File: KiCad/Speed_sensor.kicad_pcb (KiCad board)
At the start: 4 copper layers, 35 x 20 mm, 65 parts, among them J1 USB_B_Micro, J2 SWD, U1 BQ24040DSQR, U2 TP1941U, U3 ST1PS02, U4 nRF52832-QFxx, U5 LIS2DH12, Y1 32,768kHz, Y2 32MHz

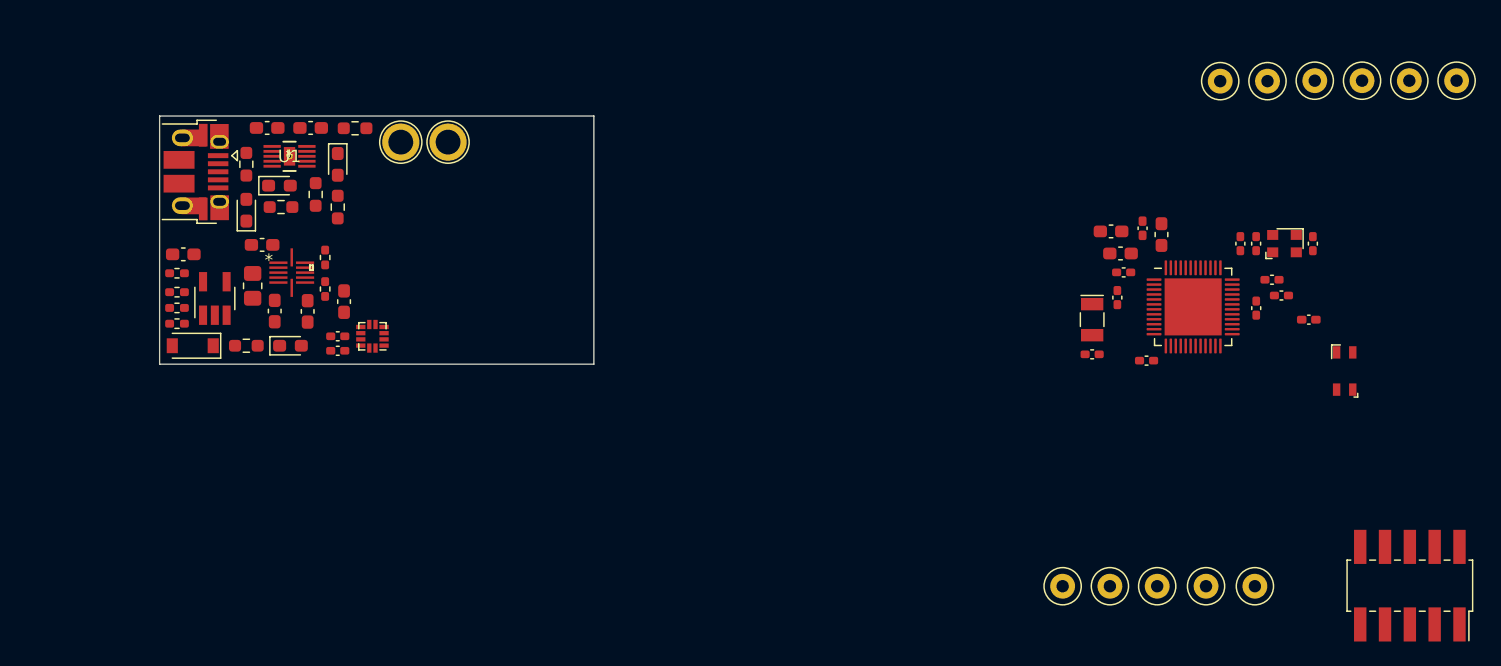
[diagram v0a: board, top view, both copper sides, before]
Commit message: kleine Änderungen an Bauteilplatzierungen um vias unterbringen zu können, 'keepout area' für Antenne eingefügt.
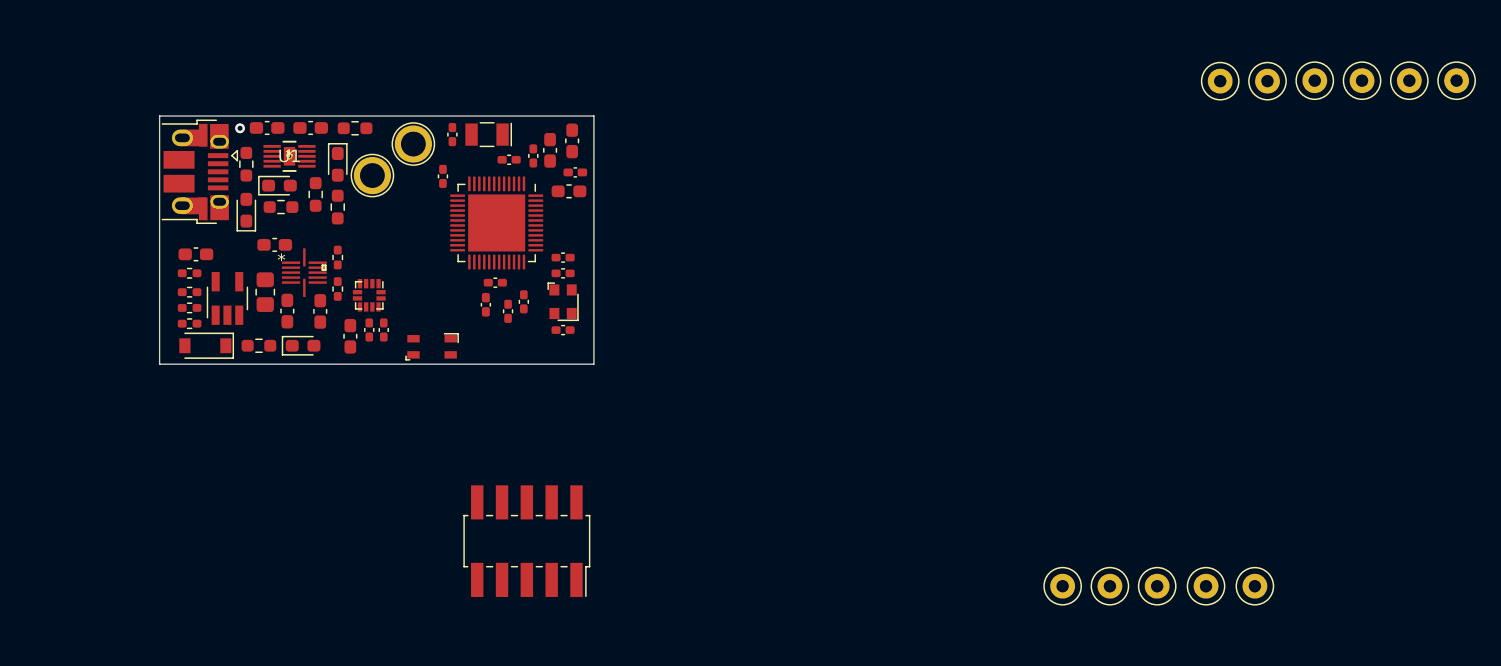
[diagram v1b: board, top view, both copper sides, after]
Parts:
- moved AE1 73.6 mm to (55.1, 55.0), turned to 180 degrees
- moved J2 71.3 mm to (62.7, 70.6)
- moved L4 66.3 mm to (59.4, 51.6), turned to 90 degrees
- moved C12 62.3 mm to (61.2, 52.1), turned to 270 degrees
- moved C17 61.4 mm to (60.2, 49.8), turned to 180 degrees
- moved C18 60.8 mm to (65.7, 53.6), turned to 180 degrees
- moved C11 60.3 mm to (62.5, 51.3), turned to 270 degrees
- moved C9 58.6 mm to (56.0, 41.2), turned to 90 degrees
- moved Y2 58.3 mm to (65.7, 51.3), turned to 90 degrees
- moved U4 56.5 mm to (60.3, 45.0), turned to 270 degrees
- moved C19 55.9 mm to (65.7, 49.0), turned to 0 degrees
- moved C10 54.6 mm to (65.7, 47.8), turned to 0 degrees
- moved C16 54.5 mm to (56.7, 37.8), turned to 90 degrees
- moved Y1 51.0 mm to (59.5, 37.8), turned to 180 degrees
- moved C15 50.3 mm to (61.3, 39.9), turned to 0 degrees
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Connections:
- U4 pad 15: Net-(U4-Pad15) -> SPI_MOSI
- U4 pad 16: SPI_MOSI -> SPI_MISO
- U4 pad 17: SPI_MISO -> SPI_01_CS
- U4 pad 18: SPI_01_CS -> SPI_SCK
- U4 pad 19: SPI_SCK -> ACCEL_INT1
- U4 pad 20: Net-(U4-Pad20) -> ACCEL_INT2
- U4 pad 8: ACCEL_INT1 -> Net-(U4-Pad8)
- U4 pad 9: ACCEL_INT2 -> Net-(U4-Pad9)
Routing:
- net +5V: vias 0 -> 1
- added copper zone on In2.Cu, net +3V0
- added copper zone on In1.Cu, net +5V
- added copper zone on In2.Cu, net +5V
- added copper zone on In2.Cu, net +BATT
- added copper zone on In1.Cu, net GND

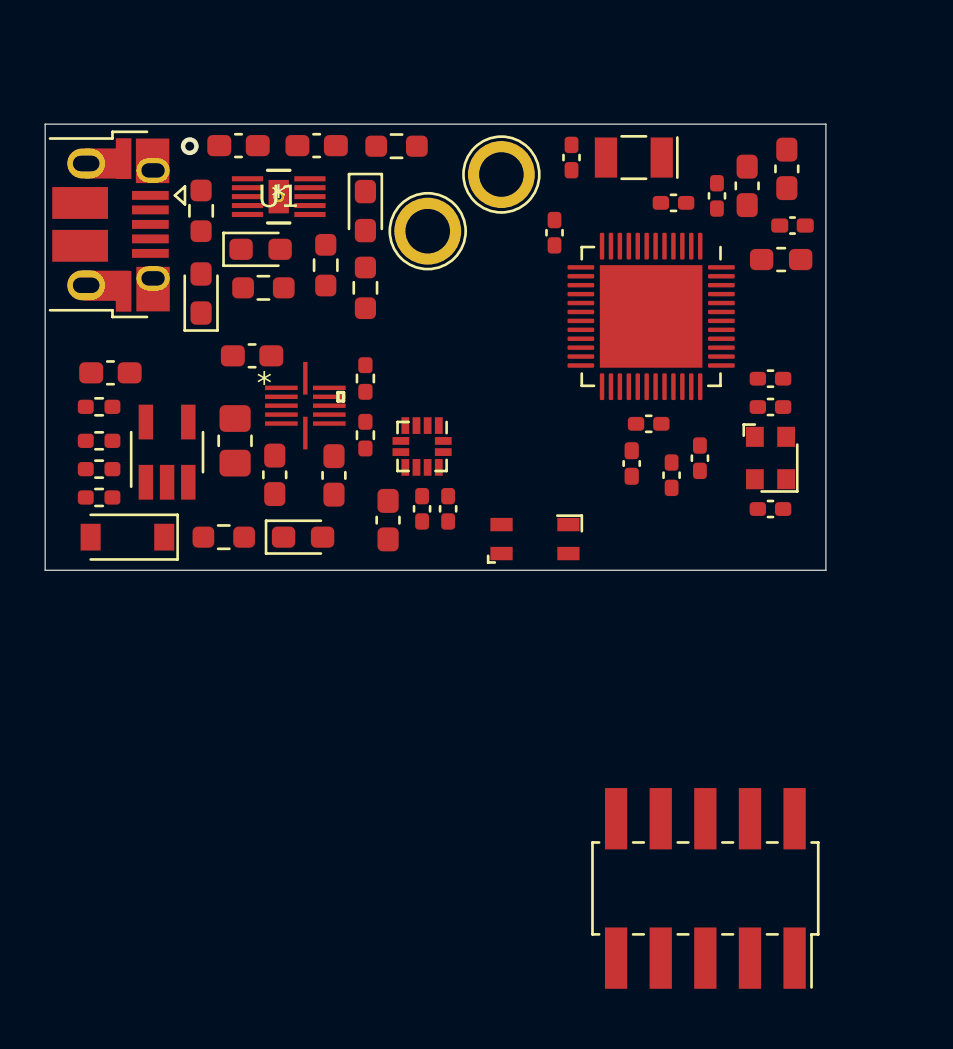
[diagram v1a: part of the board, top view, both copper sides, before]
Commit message: Änderungen nach Treffen mit Manu, opamp für alle Fälle, opamp footprint geändert, C footprint in impedance matching circuit hinzugefügt, SWD connector footprint geändert.
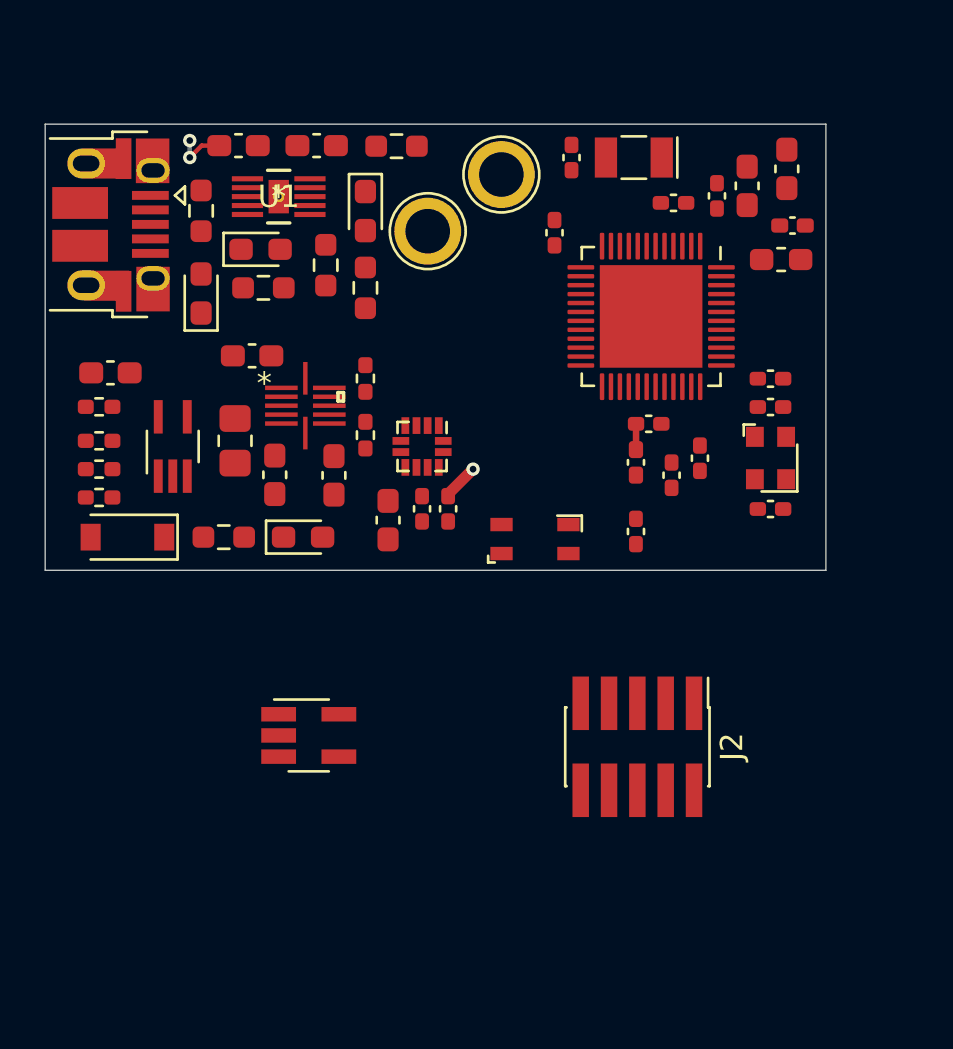
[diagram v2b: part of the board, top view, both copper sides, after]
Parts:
- added C22: N.C., Capacitor_SMD:C_0402_1005Metric_Pad0.74x0.62mm_HandSolder, F.Cu at (59.6, 54.6)
- added U6: TP1941U, Package_TO_SOT_SMD:SOT-353_SC-70-5_Handsoldering, F.Cu at (38.9, 50.8)
- J2: footprint Connector_PinSocket_2.00mm:PinSocket_2x05_P2.00mm_Vertical_SMD -> Connector_PinHeader_1.27mm:PinHeader_2x05_P1.27mm_Vertical_SMD
- U2: value TP1941U -> OPAMP
- moved U2 14.2 mm to (45.0, 63.8), turned to 0 degrees
- moved J2 7.04 mm to (59.7, 64.3)
- moved L4 0.20 mm to (59.6, 51.5)
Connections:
- U2 pad 1: Net-(R7-Pad2) -> Net-(U2-Pad1)
- U2 pad 2: GND -> Net-(U2-Pad2)
- U2 pad 3: Net-(D4-Pad1) -> Net-(U2-Pad3)
- U2 pad 4: EN -> +3V0
- U2 pad 5: +BATT -> GND
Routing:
- net +5V: track 0.00 -> 2.31 mm, vias 1 -> 2
- net +3V0: track 0.00 -> 1.67 mm, vias 0 -> 1
- net Net-(C17-Pad2): track 0.00 -> 1.16 mm

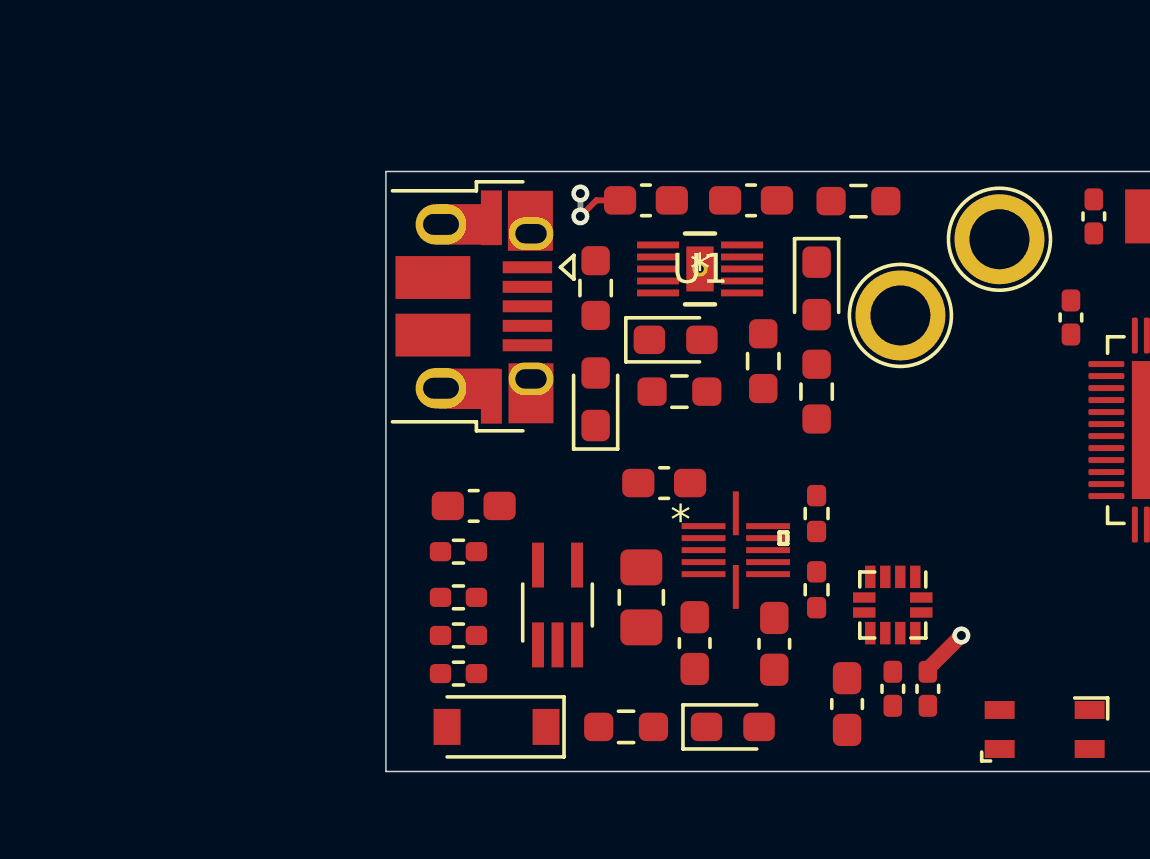
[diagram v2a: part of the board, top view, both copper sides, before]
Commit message: upgrade auf USB-C connector & footprint
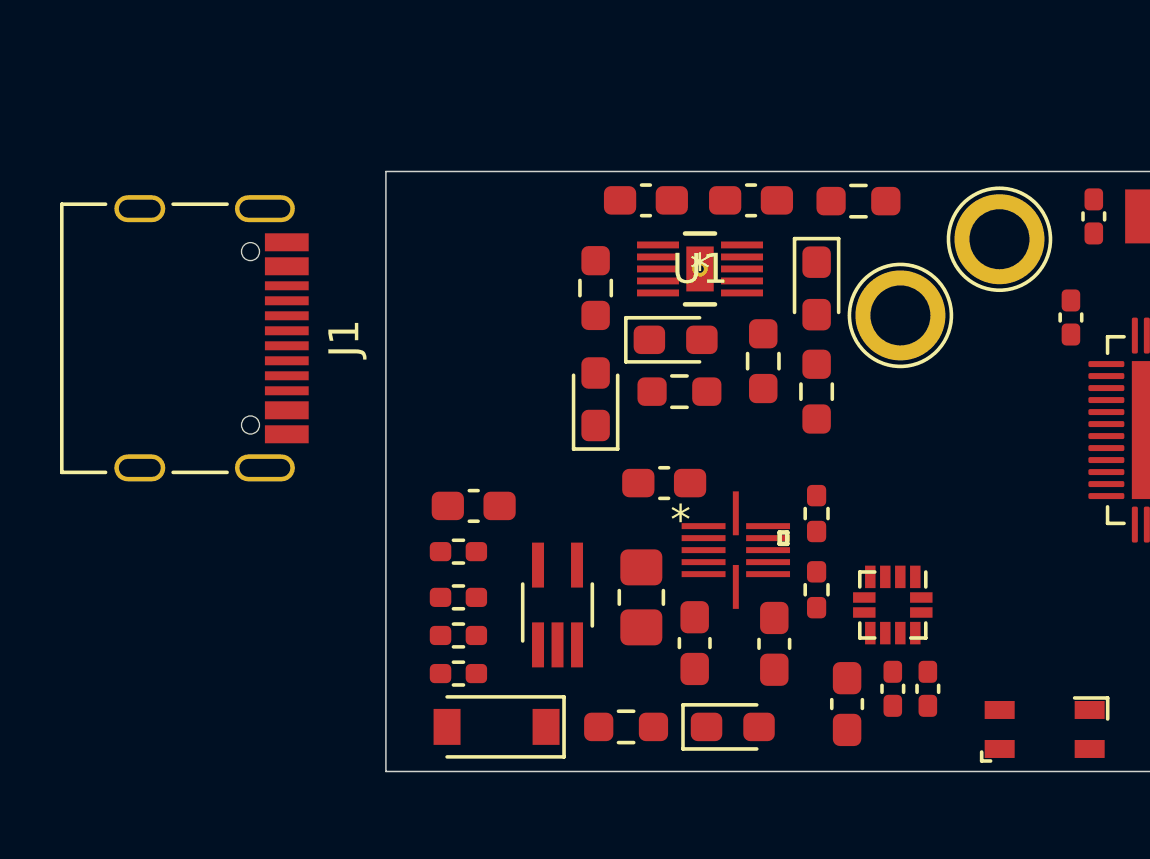
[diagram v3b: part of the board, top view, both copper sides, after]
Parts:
- J1: value USB_B_Micro -> USB_C_Receptacle_USB2.0; footprint Connector_USB:USB_Micro-B_Amphenol_10103594-0001LF_Horizontal -> myparts:USB_C_Receptacle_Palconn_UTC16-G_breitePins
- moved J1 8.98 mm to (27.2, 41.9)
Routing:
- net +5V: track 2.31 -> 0.00 mm, vias 2 -> 0
- net +3V0: track 1.67 -> 0.00 mm, vias 1 -> 0
- removed copper zone on In2.Cu, net +3V0
- removed copper zone on In1.Cu, net +5V
- removed copper zone on In2.Cu, net +5V
- removed copper zone on In2.Cu, net +BATT
- removed copper zone on In1.Cu, net GND

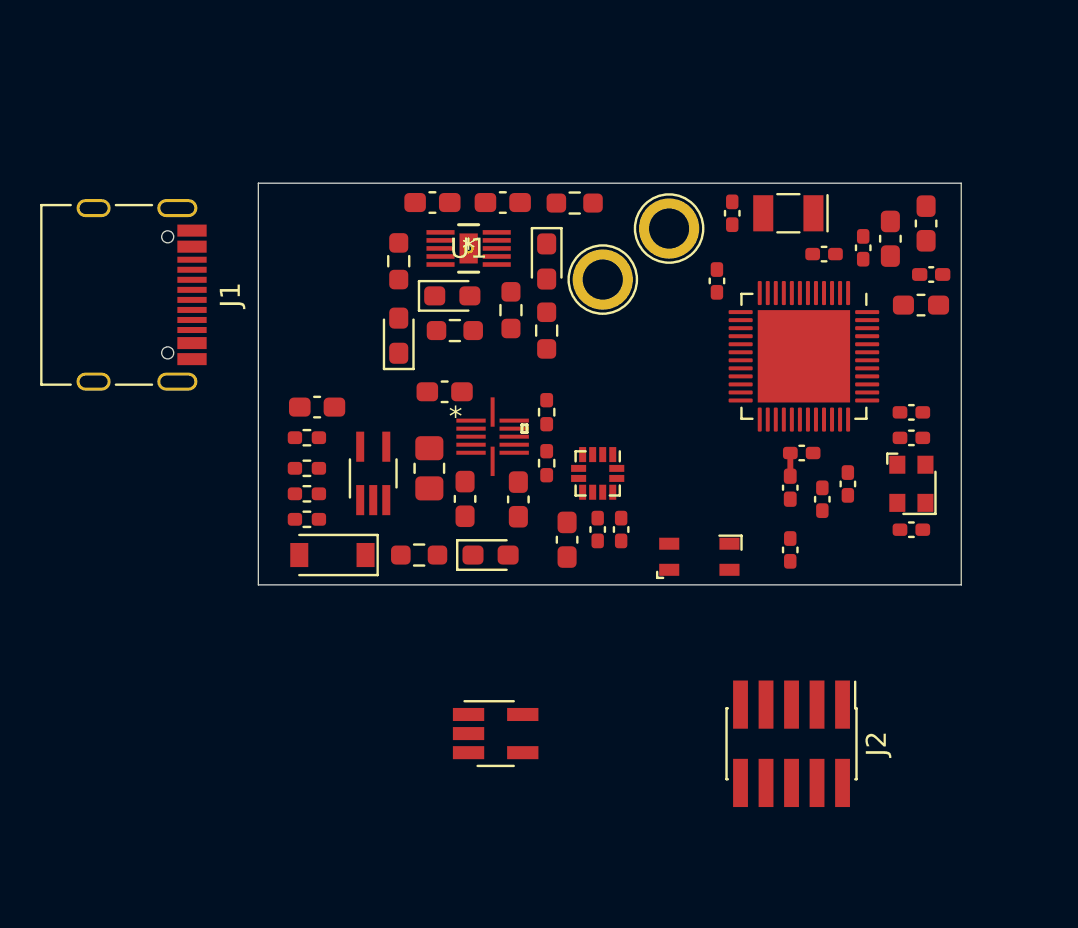
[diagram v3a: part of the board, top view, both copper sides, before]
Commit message: buck converter footprint pads verkleinert, nrf + naheliegende bauteile gedreht eingefügt, Antenne neu platziert
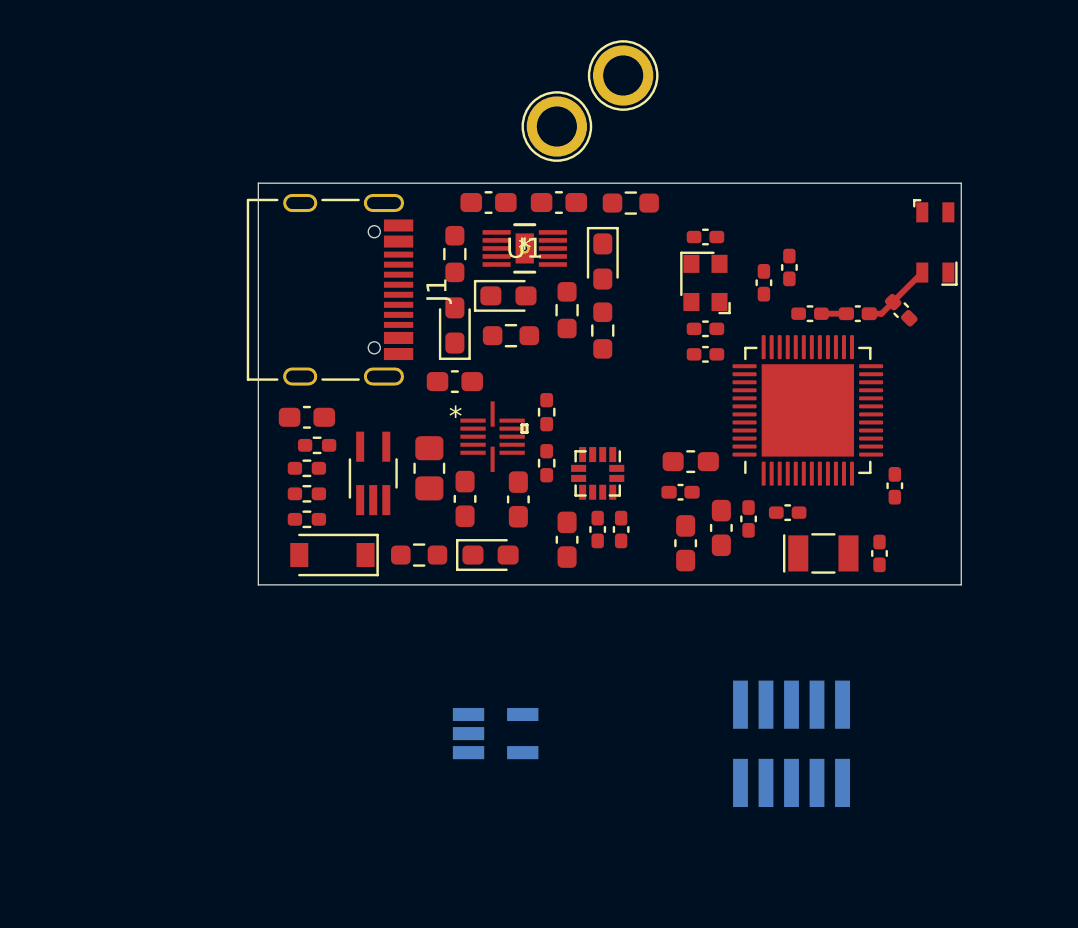
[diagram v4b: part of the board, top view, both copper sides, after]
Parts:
- AE1: value 2450AT18D0100E -> 2450AT18D0100E_right
- J2, U2: moved to B.Cu
- moved C14 19.9 mm to (54.4, 54.3), turned to 270 degrees
- moved AE1 19.6 mm to (66.8, 39.3), turned to 90 degrees
- moved C16 18.5 mm to (64.1, 54.8), turned to 270 degrees
- moved C18 17.8 mm to (55.4, 39.0), turned to 0 degrees
- moved Y1 17.0 mm to (61.3, 54.8), turned to 0 degrees
- moved C8 16.7 mm to (56.2, 53.5), turned to 270 degrees
- moved L2 16.5 mm to (54.2, 51.7), turned to 0 degrees
- moved C13 14.7 mm to (57.5, 53.1), turned to 270 degrees
- moved Y2 14.3 mm to (55.4, 41.3), turned to 270 degrees
- moved L3 13.9 mm to (54.7, 50.2), turned to 180 degrees
- moved C9 13.5 mm to (64.8, 51.4), turned to 270 degrees
- moved C22 13.2 mm to (65.2, 42.7), turned to 135 degrees
- moved C15 13.0 mm to (59.5, 52.8), turned to 180 degrees
- moved C12 11.7 mm to (59.6, 40.5), turned to 90 degrees
- moved C19 11.6 mm to (55.4, 43.6), turned to 180 degrees
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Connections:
- AE1 pad 1: Net-(AE1-Pad1) -> GND
- AE1 pad 4: GND -> Net-(AE1-Pad4)
- C22 pad 2: Net-(AE1-Pad1) -> Net-(AE1-Pad4)
- L4 pad 1: Net-(AE1-Pad1) -> Net-(AE1-Pad4)
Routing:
- net Net-(AE1-Pad4): track 0.00 -> 3.50 mm
- added copper zone on In1.Cu, net GND
